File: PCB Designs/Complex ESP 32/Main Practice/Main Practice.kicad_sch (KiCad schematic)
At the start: 25 parts, among them J1 SS-52400-002, J2 B2B-PH-SM4-TB, U1 MCP73871

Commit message: Developed upon esp 32 schem
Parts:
- C1, C2, C5, C6: footprint (none) -> Capacitor_SMD:C_0805_2012Metric
- C3, C4: footprint (none) -> Footprints:T491A
- F1: footprint FUSC3226X100N -> Footprints:FUSC3226X100N
- J1: Availability In Stock -> (none); Package None -> (none); Price None -> (none)
- J2: Availability In Stock -> (none); Package NON STANDARD-2 JST -> (none); Price None -> (none)
- LED1, LED2, LED3, LED4: footprint LEDC2012X120N -> Footprints:LEDC2012X120N
- R1, R10, R2, R3, R4, R5, R6, R7, R8, R9: footprint (none) -> Resistor_SMD:R_0805_2012Metric
- VR1: Availability In Stock -> (none); Package SOT-223-4 ON Semiconductor -> (none); Price None -> (none)
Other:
- sheet ESP 32 C3 02 ports: added USB_DN, USB_DP, VBUS; removed none
- note added: "Battery JST Connector"
- note added: "LiPo Battery Charger"
- note added: "Low Drop Out LDO"
- note added: "Power LED"
- note added: "USB-C Connector"

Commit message: Saved UI
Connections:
- net GND: now also U1.3 (SEL)

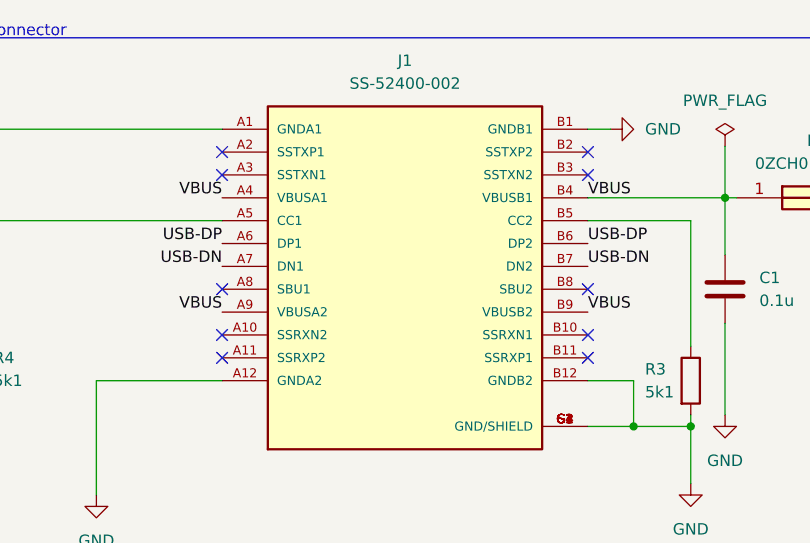
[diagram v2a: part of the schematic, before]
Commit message: Started Schematics of footprint
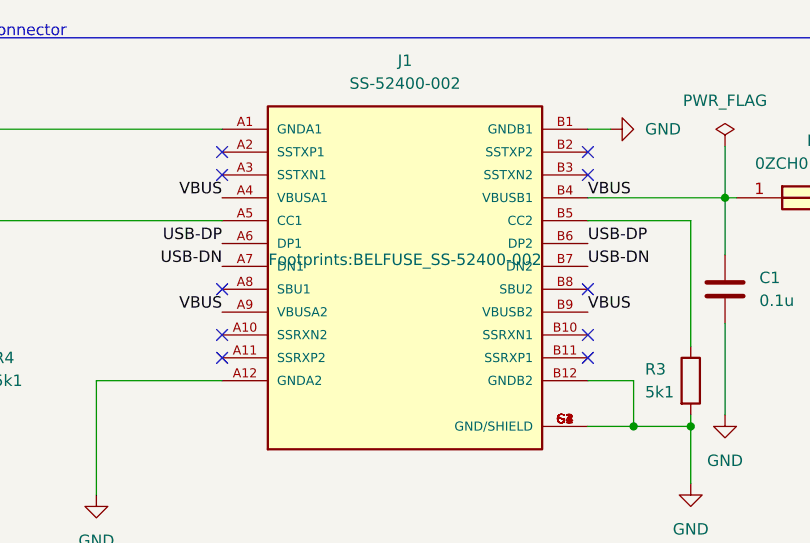
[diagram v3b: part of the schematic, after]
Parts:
- J1: footprint SS-52400-002:BELFUSE_SS-52400-002 -> Footprints:BELFUSE_SS-52400-002
- J2: footprint B2B-PH-SM4-TB:JST_B2B-PH-SM4-TB -> Footprints:JST_B2B-PH-SM4-TB
- VR1: footprint LM1117MPX-3.3:VREG_LM1117MPX-3.3 -> Footprints:VREG_LM1117MPX-3.3
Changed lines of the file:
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@@
 			)
 		)
-		(property "Footprint" "SS-52400-002:BELFUSE_SS-52400-002"
+		(property "Footprint" "Footprints:BELFUSE_SS-52400-002"
 			(at 76.2 44.45 0)
-			(hide yes)
 			(show_name no)
 			(do_not_autoplace no)
@@
 			)
 		)
-		(property "Footprint" "LM1117MPX-3.3:VREG_LM1117MPX-3.3"
+		(property "Footprint" "Footprints:VREG_LM1117MPX-3.3"
 			(at 71.12 104.14 0)
 			(hide yes)
@@
 			)
 		)
-		(property "Footprint" "B2B-PH-SM4-TB:JST_B2B-PH-SM4-TB"
+		(property "Footprint" "Footprints:JST_B2B-PH-SM4-TB"
 			(at 36.83 134.62 0)
 			(hide yes)
